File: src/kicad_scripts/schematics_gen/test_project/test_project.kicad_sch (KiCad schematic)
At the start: 101 parts

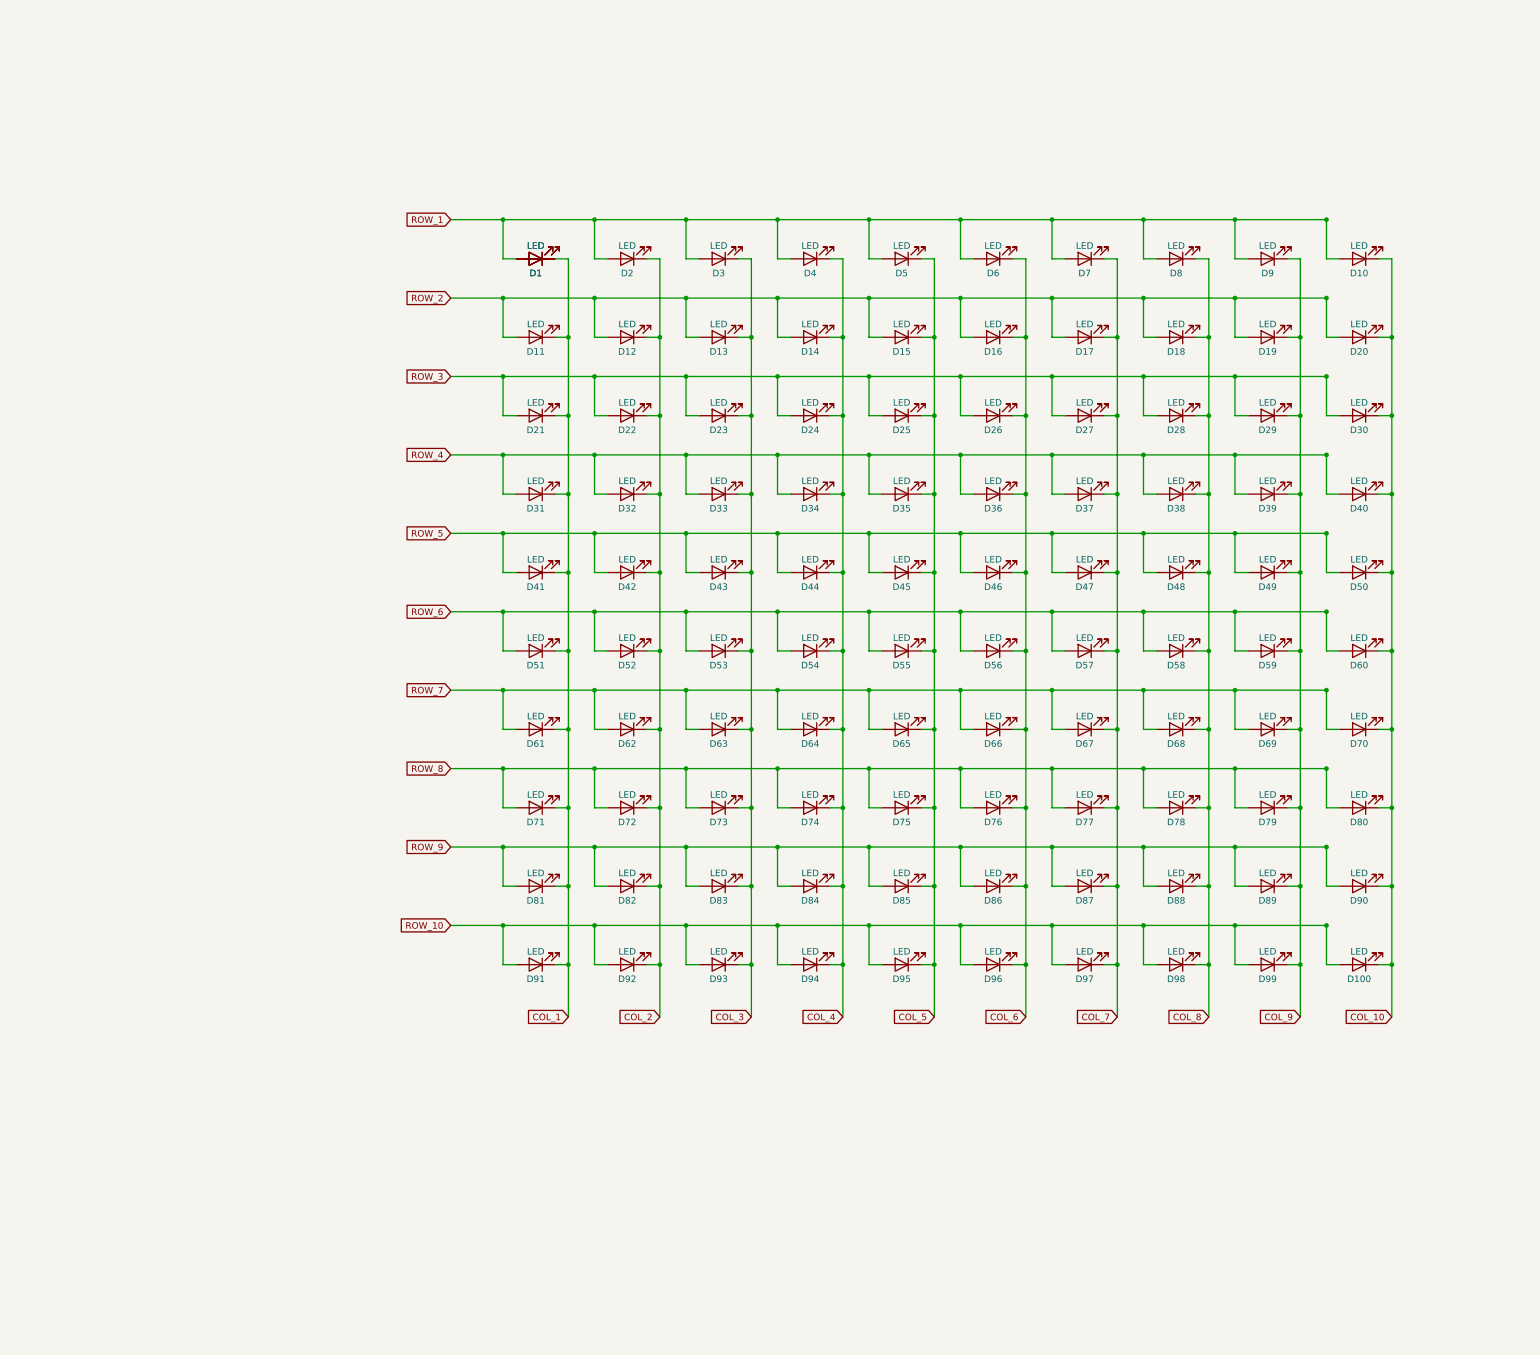
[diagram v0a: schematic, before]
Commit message: Added basic classed compenent Matrix Maker
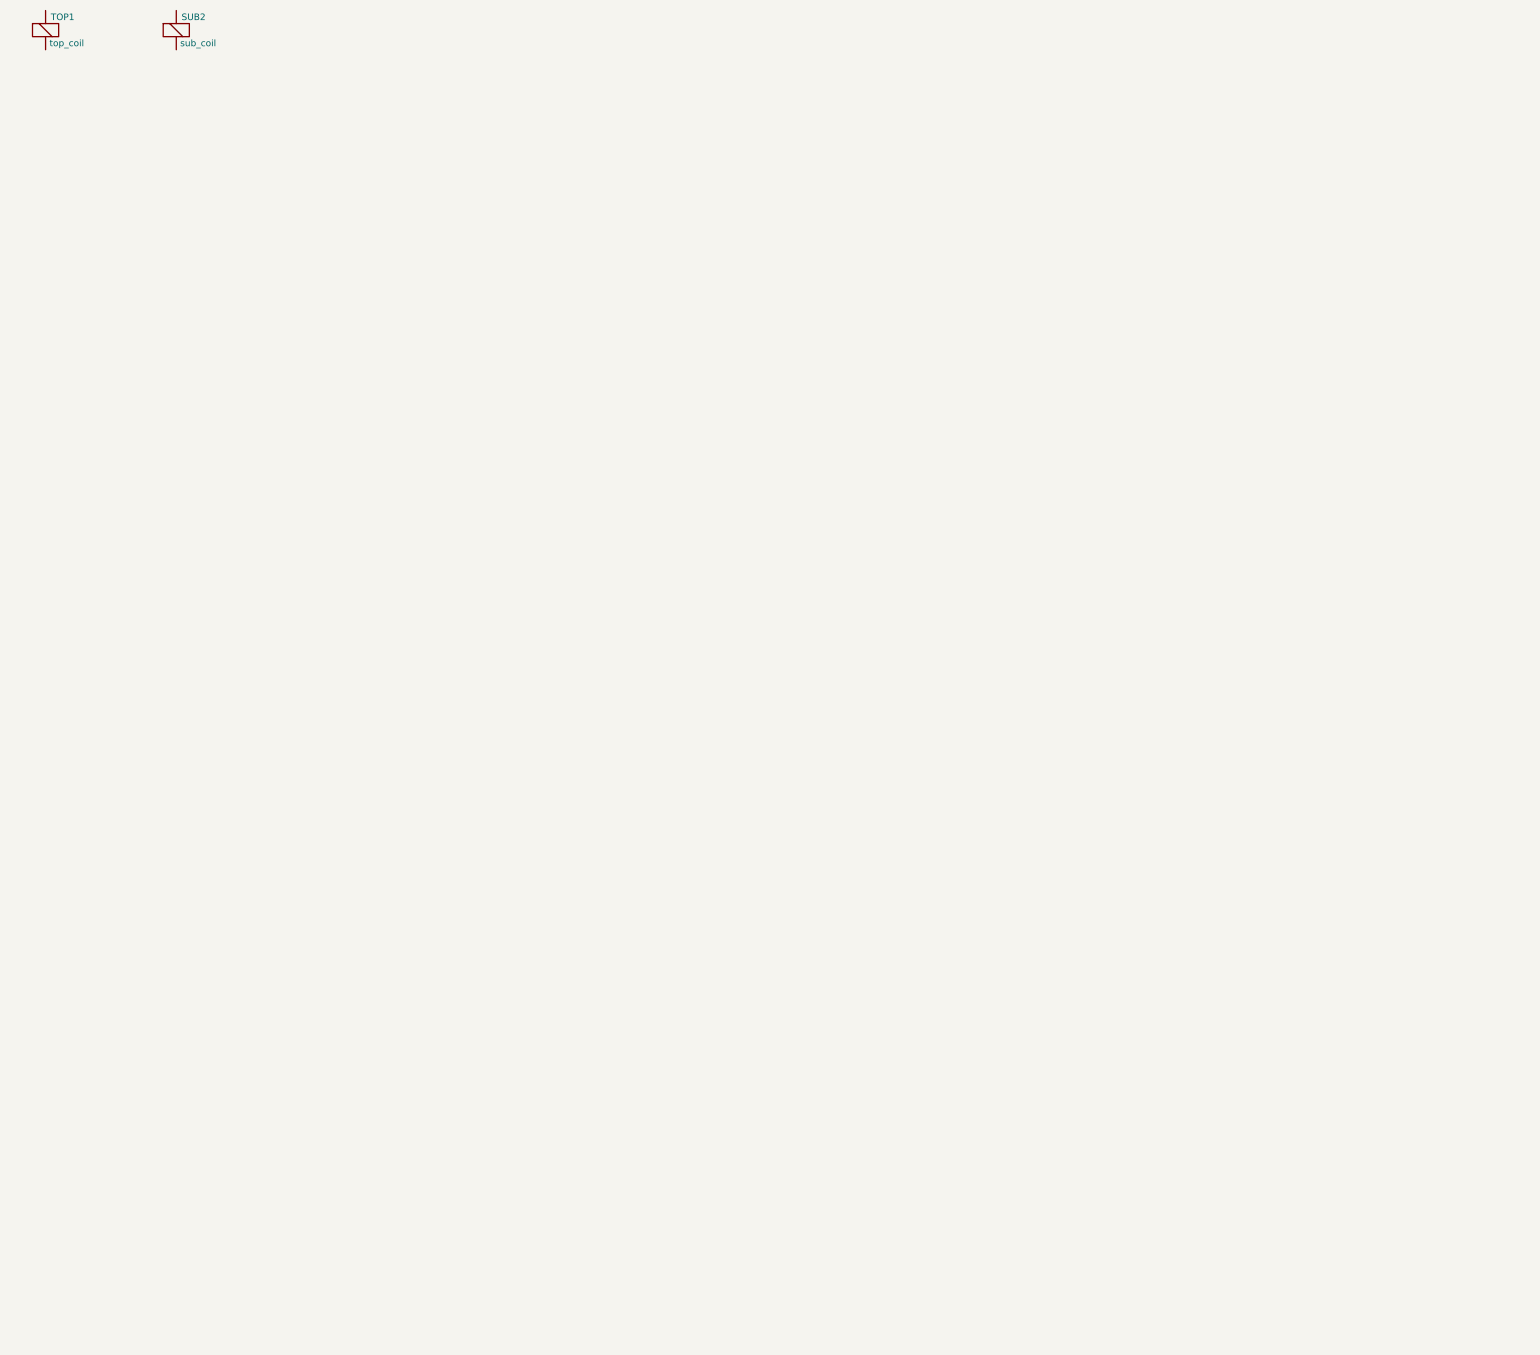
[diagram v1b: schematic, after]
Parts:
- removed D1 (x2), D10, D100, D11, D12, D13, D14, D15, D16, D17, D18, D19, D2, D20, D21, D22, D23, D24, D25, D26, D27, D28, D29, D3, D30, D31, D32, D33, D34, D35, D36, D37, D38, D39, D4, D40, D41, D42, D43, D44, D45, D46, D47, D48, D49, D5, D50, D51, D52, D53, D54, D55, D56, D57, D58, D59, D6, D60, D61, D62, D63, D64, D65, D66, D67, D68, D69, D7, D70, D71, D72, D73, D74, D75, D76, D77, D78, D79, D8, D80, D81, D82, D83, D84, D85, D86, D87, D88, D89, D9, D90, D91, D92, D93, D94, D95, D96, D97, D98, D99: LED, symbol Device:LED
- added SUB2: sub_coil, sub_coils:sub_coil, symbol Device:ElectromagneticActor
- added TOP1: top_coil, sub_coils:top_coil, symbol Device:ElectromagneticActor
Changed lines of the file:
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@@
+(kicad_sch
+	(version 20231120)
+	(generator "eeschema")
+	(generator_version "8.0")
+	(paper "A3")
+	(symbol
+		(lib_id "Device:ElectromagneticActor")
+		(at -25.4 -17.78 0)
+		(unit 1)
+		(exclude_from_sim no)
+		(in_bom yes)
+		(on_board yes)
+		(dnp no)
+		(property "Reference" "SUB2"
+			(at -24.384 -21.59 0)
+			(effects
+				(font
+					(size 1.27 1.27)
+				)
+				(justify left)
+			)
+		)
+		(property "Value" "sub_coil"
+			(at -24.638 -16.51 0)
+			(effects
+				(font
+					(size 1.27 1.27)
+				)
+				(justify left)
+			)
+		)
+		(property "Footprint" "sub_coils:sub_coil"
+			(at -26.035 -20.32 90)
+			(effects
+				(font
+					(size 1.27 1.27)
+				)
+				(hide yes)
+			)
+		)
+		(property "Datasheet" "~"
+			(at -26.035 -20.32 90)
+			(effects
+				(font
+					(size 1.27 1.27)
+				)
+				(hide yes)
+			)
+		)
+		(property "Description" "Electromagnetic actor"
+			(at -25.4 -17.78 0)
+			(effects
+				(font
+					(size 1.27 1.27)
+				)
+				(hide yes)
+			)
+		)
+		(pin "2"
+		)
+		(pin "1"
+		)
+		(instances
+			(project "test_project"
+				(path "/11af7b42-8094-4ca6-9444-8e07a1921bec"
+					(reference "SUB2")
+					(unit 1)
+				)
+			)
+		)
+	)
+	(symbol
+		(lib_id "Device:ElectromagneticActor")
+		(at -50.8 -17.78 0)
+		(unit 1)
+		(exclude_from_sim no)
+		(in_bom yes)
+		(on_board yes)
+		(dnp no)
+		(property "Reference" "TOP1"
+			(at -49.784 -21.59 0)
+			(effects
+				(font
+					(size 1.27 1.27)
+				)
+				(justify left)
+			)
+		)
+		(property "Value" "top_coil"
+			(at -50.038 -16.51 0)
+			(effects
+				(font
+					(size 1.27 1.27)
+				)
+				(justify left)
+			)
+		)
+		(property "Footprint" "sub_coils:top_coil"
+			(at -51.435 -20.32 90)
+			(effects
+				(font
+					(size 1.27 1.27)
+				)
+				(hide yes)
+			)
+		)
+		(property "Datasheet" "~"
+			(at -51.435 -20.32 90)
+			(effects
+				(font
+					(size 1.27 1.27)
+				)
+				(hide yes)
+			)
+		)
+		(property "Description" "Electromagnetic actor"
+			(at -50.8 -17.78 0)
+			(effects
+				(font
+					(size 1.27 1.27)
+				)
+				(hide yes)
+			)
+		)
+		(pin "2"
+		)
+		(pin "1"
+		)
+		(instances
+			(project "test_project"
+				(path "/11af7b42-8094-4ca6-9444-8e07a1921bec"
+					(reference "TOP1")
+					(unit 1)
+				)
+			)
+		)
+	)
+	(sheet_instances
+		(path "/"
+			(page "1")
+		)
+	)
+)

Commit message: Before turning components in schematics maker
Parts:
- removed SUB2: sub_coil, sub_coils:sub_coil, symbol Device:ElectromagneticActor
- removed TOP1: top_coil, sub_coils:top_coil, symbol Device:ElectromagneticActor
- added SUB1, SUB10, SUB11, SUB12, SUB13, SUB14, SUB15, SUB16, SUB17, SUB18, SUB19, SUB2, SUB20, SUB21, SUB22, SUB23, SUB24, SUB25, SUB26, SUB27, SUB28, SUB29, SUB3, SUB30, SUB31, SUB32, SUB33, SUB34, SUB35, SUB36, SUB37, SUB38, SUB39, SUB4, SUB40, SUB41, SUB42, SUB43, SUB44, SUB45, SUB46, SUB47, SUB48, SUB49, SUB5, SUB50, SUB51, SUB6, SUB7, SUB8, SUB9: sub_coil, sub_coils:top_coil, symbol square_coils:sub_coil
- added TOP1 (x2), TOP10, TOP11, TOP12, TOP13, TOP14, TOP15, TOP16, TOP17, TOP18, TOP19, TOP2, TOP20, TOP21, TOP22, TOP23, TOP24, TOP25, TOP26, TOP27, TOP28, TOP29, TOP3, TOP30, TOP31, TOP32, TOP33, TOP34, TOP35, TOP36, TOP37, TOP38, TOP39, TOP4, TOP40, TOP41, TOP42, TOP43, TOP44, TOP45, TOP46, TOP47, TOP48, TOP49, TOP5, TOP50, TOP6, TOP7, TOP8, TOP9: top_coil, sub_coils:top_coil, symbol square_coils:top_coil
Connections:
- new net COL_1: SUB1.1 (A), SUB1.2 (B), SUB10.1 (A), SUB10.2 (B), SUB11.1 (A), SUB11.2 (B), SUB12.1 (A), SUB12.2 (B), SUB13.1 (A), SUB13.2 (B), SUB14.1 (A), SUB14.2 (B), SUB15.1 (A), SUB15.2 (B), SUB16.1 (A), SUB16.2 (B), SUB17.1 (A), SUB17.2 (B), SUB18.1 (A), SUB18.2 (B), SUB19.1 (A), SUB19.2 (B), SUB2.1 (A), SUB2.2 (B), SUB20.1 (A), SUB20.2 (B), SUB21.1 (A), SUB21.2 (B), SUB22.1 (A), SUB22.2 (B), SUB23.1 (A), SUB23.2 (B), SUB24.1 (A), SUB24.2 (B), SUB25.1 (A), SUB25.2 (B), SUB26.1 (A), SUB26.2 (B), SUB27.1 (A), SUB27.2 (B), SUB28.1 (A), SUB28.2 (B), SUB29.1 (A), SUB29.2 (B), SUB3.1 (A), SUB3.2 (B), SUB30.1 (A), SUB30.2 (B), SUB31.1 (A), SUB31.2 (B), SUB32.1 (A), SUB32.2 (B), SUB33.1 (A), SUB33.2 (B), SUB34.1 (A), SUB34.2 (B), SUB35.1 (A), SUB35.2 (B), SUB36.1 (A), SUB36.2 (B), SUB37.1 (A), SUB37.2 (B), SUB38.1 (A), SUB38.2 (B), SUB39.1 (A), SUB39.2 (B), SUB4.1 (A), SUB4.2 (B), SUB40.1 (A), SUB40.2 (B), SUB41.1 (A), SUB41.2 (B), SUB42.1 (A), SUB42.2 (B), SUB43.1 (A), SUB43.2 (B), SUB44.1 (A), SUB44.2 (B), SUB45.1 (A), SUB45.2 (B), SUB46.1 (A), SUB46.2 (B), SUB47.1 (A), SUB47.2 (B), SUB48.1 (A), SUB48.2 (B), SUB49.1 (A), SUB49.2 (B), SUB5.1 (A), SUB5.2 (B), SUB50.1 (A), SUB50.2 (B), SUB6.1 (A), SUB6.2 (B), SUB7.1 (A), SUB7.2 (B), SUB8.1 (A), SUB8.2 (B), SUB9.1 (A), SUB9.2 (B), TOP1.1 (A), TOP1.2 (B), TOP10.1 (A), TOP10.2 (B), TOP11.1 (A), TOP11.2 (B), TOP12.1 (A), TOP12.2 (B), TOP13.1 (A), TOP13.2 (B), TOP14.1 (A), TOP14.2 (B), TOP15.1 (A), TOP15.2 (B), TOP16.1 (A), TOP16.2 (B), TOP17.1 (A), TOP17.2 (B), TOP18.1 (A), TOP18.2 (B), TOP19.1 (A), TOP19.2 (B), TOP2.1 (A), TOP2.2 (B), TOP20.1 (A), TOP20.2 (B), TOP21.1 (A), TOP21.2 (B), TOP22.1 (A), TOP22.2 (B), TOP23.1 (A), TOP23.2 (B), TOP24.1 (A), TOP24.2 (B), TOP25.1 (A), TOP25.2 (B), TOP26.1 (A), TOP26.2 (B), TOP27.1 (A), TOP27.2 (B), TOP28.1 (A), TOP28.2 (B), TOP29.1 (A), TOP29.2 (B), TOP3.1 (A), TOP3.2 (B), TOP30.1 (A), TOP30.2 (B), TOP31.1 (A), TOP31.2 (B), TOP32.1 (A), TOP32.2 (B), TOP33.1 (A), TOP33.2 (B), TOP34.1 (A), TOP34.2 (B), TOP35.1 (A), TOP35.2 (B), TOP36.1 (A), TOP36.2 (B), TOP37.1 (A), TOP37.2 (B), TOP38.1 (A), TOP38.2 (B), TOP39.1 (A), TOP39.2 (B), TOP4.1 (A), TOP4.2 (B), TOP40.1 (A), TOP40.2 (B), TOP41.1 (A), TOP41.2 (B), TOP42.1 (A), TOP42.2 (B), TOP43.1 (A), TOP43.2 (B), TOP44.1 (A), TOP44.2 (B), TOP45.1 (A), TOP45.2 (B), TOP46.1 (A), TOP46.2 (B), TOP47.1 (A), TOP47.2 (B), TOP48.1 (A), TOP48.2 (B), TOP49.1 (A), TOP49.2 (B), TOP5.1 (A), TOP5.2 (B), TOP50.1 (A), TOP50.2 (B), TOP6.1 (A), TOP6.2 (B), TOP7.1 (A), TOP7.2 (B), TOP8.1 (A), TOP8.2 (B), TOP9.1 (A), TOP9.2 (B)
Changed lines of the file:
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@@
-(kicad_sch
-	(version 20231120)
-	(generator "eeschema")
-	(generator_version "8.0")
-	(paper "A3")
-	(symbol
-		(lib_id "Device:ElectromagneticActor")
-		(at -25.4 -17.78 0)
-		(unit 1)
-		(exclude_from_sim no)
-		(in_bom yes)
-		(on_board yes)
-		(dnp no)
-		(property "Reference" "SUB2"
-			(at -24.384 -21.59 0)
-			(effects
-				(font
-					(size 1.27 1.27)
-				)
-				(justify left)
-			)
-		)
-		(property "Value" "sub_coil"
-			(at -24.638 -16.51 0)
-			(effects
-				(font
-					(size 1.27 1.27)
-				)
-				(justify left)
-			)
-		)
-		(property "Footprint" "sub_coils:sub_coil"
-			(at -26.035 -20.32 90)
-			(effects
-				(font
-					(size 1.27 1.27)
-				)
-				(hide yes)
-			)
-		)
-		(property "Datasheet" "~"
-			(at -26.035 -20.32 90)
-			(effects
-				(font
-					(size 1.27 1.27)
-				)
-				(hide yes)
-			)
-		)
-		(property "Description" "Electromagnetic actor"
-			(at -25.4 -17.78 0)
-			(effects
-				(font
-					(size 1.27 1.27)
-				)
-				(hide yes)
-			)
-		)
-		(pin "2"
-		)
-		(pin "1"
-		)
-		(instances
-			(project "test_project"
-				(path "/11af7b42-8094-4ca6-9444-8e07a1921bec"
-					(reference "SUB2")
-					(unit 1)
-				)
-			)
-		)
-	)
-	(symbol
-		(lib_id "Device:ElectromagneticActor")
-		(at -50.8 -17.78 0)
-		(unit 1)
-		(exclude_from_sim no)
-		(in_bom yes)
-		(on_board yes)
-		(dnp no)
-		(property "Reference" "TOP1"
-			(at -49.784 -21.59 0)
-			(effects
-				(font
-					(size 1.27 1.27)
-				)
-				(justify left)
-			)
-		)
-		(property "Value" "top_coil"
-			(at -50.038 -16.51 0)
-			(effects
-				(font
-					(size 1.27 1.27)
-				)
-				(justify left)
-			)
-		)
-		(property "Footprint" "sub_coils:top_coil"
-			(at -51.435 -20.32 90)
-			(effects
-				(font
-					(size 1.27 1.27)
-				)
-				(hide yes)
-			)
-		)
-		(property "Datasheet" "~"
-			(at -51.435 -20.32 90)
-			(effects
-				(font
-					(size 1.27 1.27)
-				)
-				(hide yes)
-			)
-		)
-		(property "Description" "Electromagnetic actor"
-			(at -50.8 -17.78 0)
-			(effects
-				(font
-					(size 1.27 1.27)
-				)
-				(hide yes)
-			)
-		)
-		(pin "2"
-		)
-		(pin "1"
-		)
-		(instances
-			(project "test_project"
-				(path "/11af7b42-8094-4ca6-9444-8e07a1921bec"
-					(reference "TOP1")
-					(unit 1)
-				)
-			)
-		)
-	)
-	(sheet_instances
-		(path "/"
-			(page "1")
-		)
-	)
-)
